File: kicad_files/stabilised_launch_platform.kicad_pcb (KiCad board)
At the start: 2 copper layers, 83.1 x 64.6 mm, 37 parts, among them J1 Conn_01x03_Male, J2 Conn_01x03_Male, J3 Conn_01x06_Male, J4 USB_C_Receptacle_USB2.0, SW1 SW_Push, U1 MAX7375AXR805, U2 AP7370-33Y, U3 STM32L011F3Px, U4 FT201XS, U5 LIS3DH

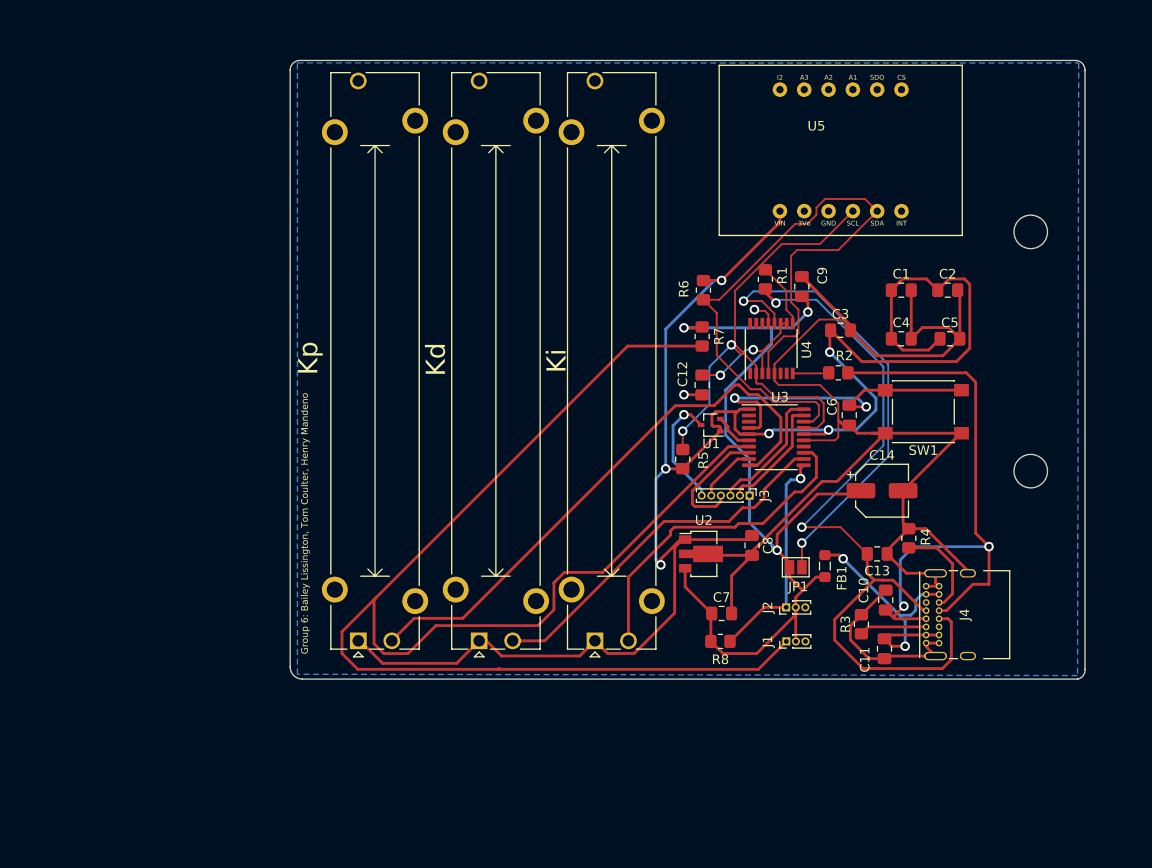
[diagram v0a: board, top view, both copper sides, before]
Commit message: fixed footprints, added mounting holes, fixed traces
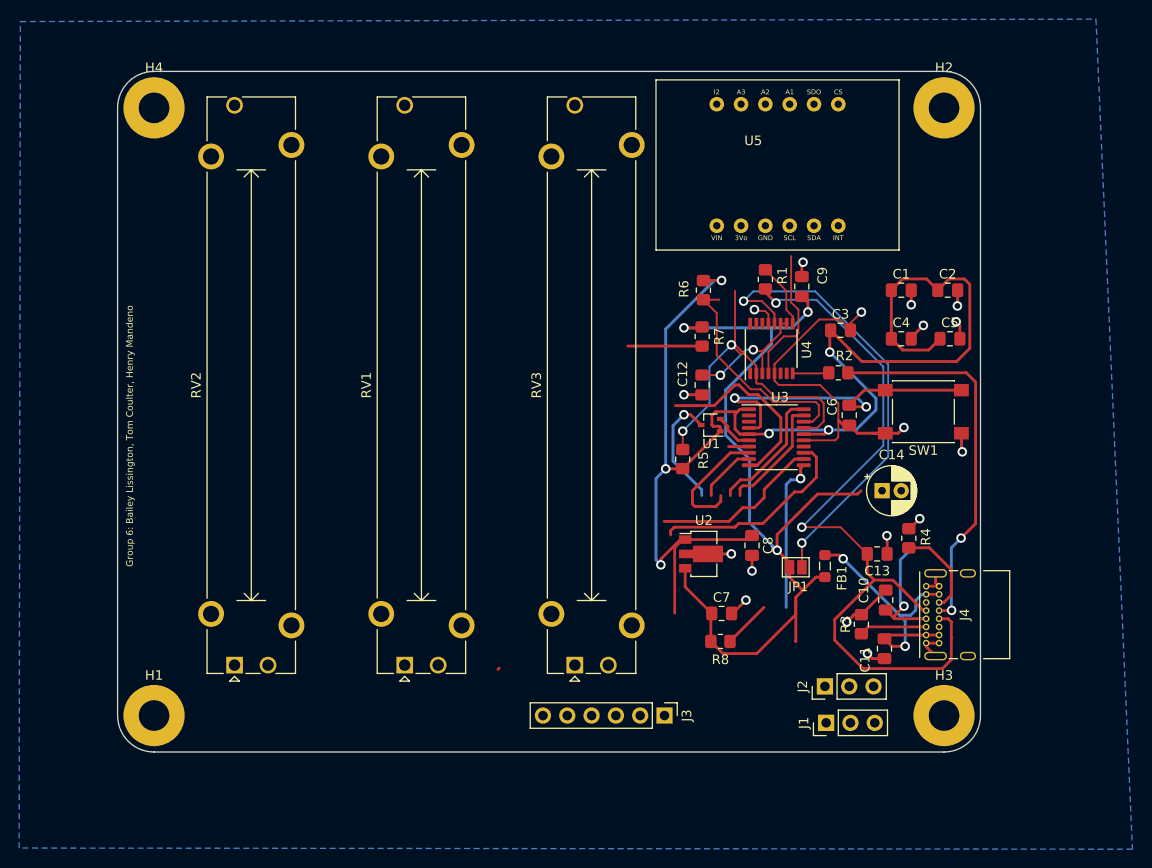
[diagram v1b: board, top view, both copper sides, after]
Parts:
- removed Kd, Ki, Kp: R_Potentiometer, Potentiometer_THT:Potentiometer_Bourns_PTA4543_Single_Slide
- added H1: MountingHole_Pad, MountingHole:MountingHole_3.2mm_M3_Pad, F.Cu at (72.4, 129.5)
- added H2: MountingHole_Pad, MountingHole:MountingHole_3.2mm_M3_Pad, F.Cu at (154.9, 66.0)
- added H3: MountingHole_Pad, MountingHole:MountingHole_3.2mm_M3_Pad, F.Cu at (154.9, 129.5)
- added H4: MountingHole_Pad, MountingHole:MountingHole_3.2mm_M3_Pad, F.Cu at (72.4, 66.0)
- added RV1: R_Potentiometer, Potentiometer_THT:Potentiometer_Bourns_PTA4543_Single_Slide, F.Cu at (98.6, 124.3)
- added RV2: R_Potentiometer, Potentiometer_THT:Potentiometer_Bourns_PTA4543_Single_Slide, F.Cu at (80.8, 124.3)
- added RV3: R_Potentiometer, Potentiometer_THT:Potentiometer_Bourns_PTA4543_Single_Slide, F.Cu at (116.4, 124.3)
- C14: footprint Capacitor_SMD:CP_Elec_5x3 -> Capacitor_THT:CP_Radial_D5.0mm_P2.00mm
- J1, J2: footprint Connector_PinHeader_1.00mm:PinHeader_1x03_P1.00mm_Vertical -> Connector_PinHeader_2.54mm:PinHeader_1x03_P2.54mm_Vertical
- J3: footprint Connector_PinHeader_1.00mm:PinHeader_1x06_P1.00mm_Vertical -> Connector_PinHeader_2.54mm:PinHeader_1x06_P2.54mm_Vertical
- moved J3 24.6 mm to (125.7, 129.5)
- moved J1 9.47 mm to (142.6, 130.3)
- moved J2 9.19 mm to (142.5, 126.5)
- moved U5 6.78 mm to (137.5, 72.0)
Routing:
- net SERVO1_SIG: track 155.8 -> 10.1 mm
- net GND: track 184.9 -> 93.5 mm, vias 3 -> 18
- net +3.3V: track 192.0 -> 143.7 mm
- net POT1: track 60.0 -> 20.2 mm
- net SDA: track 71.2 -> 38.4 mm
- net POT2: track 38.8 -> 17.8 mm
- net SCL: track 53.3 -> 37.5 mm
- net POT3: track 34.5 -> 21.6 mm
- net USBDP: track 63.0 -> 53.3 mm, vias 2 -> 3
- net SERVO2_SIG: track 23.5 -> 21.2 mm
- net Net-(J4-PadB5): track 10.2 -> 9.64 mm
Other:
- board size 83.1 x 64.6 mm -> 90.2 x 71.1 mm

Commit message: PCB routing finished
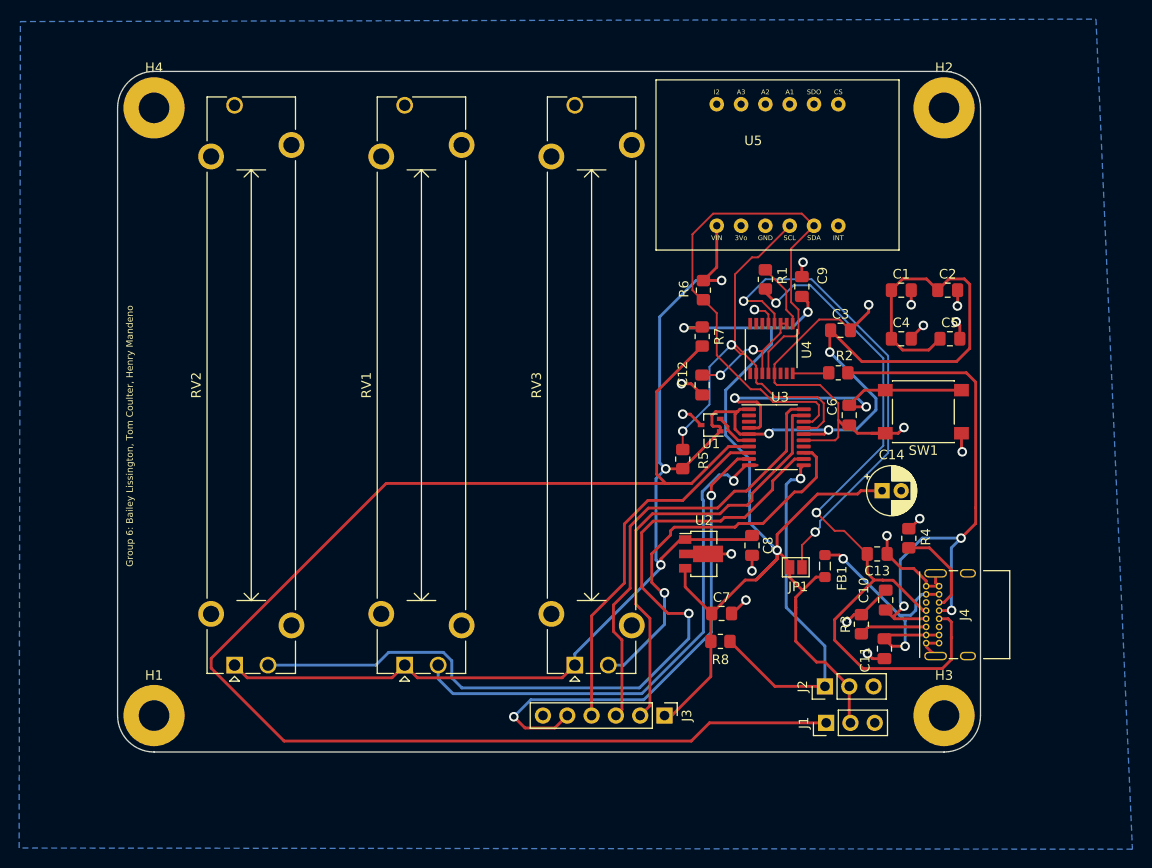
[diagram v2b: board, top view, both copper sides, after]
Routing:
- net SERVO1_SIG: track 10.1 -> 151.6 mm
- net POT2: track 17.8 -> 84.3 mm, vias 0 -> 1
- net +3.3V: track 143.7 -> 195.6 mm
- net MCU_RX: track 6.15 -> 51.3 mm, vias 0 -> 2
- net POT1: track 20.2 -> 54.8 mm, vias 0 -> 1
- net SWDIO: track 12.4 -> 45.6 mm
- net SWCLK: track 13.6 -> 46.6 mm
- net +5V: track 92.5 -> 119.3 mm
- net MCU_TX: track 12.8 -> 37.5 mm
- net SDA: track 38.4 -> 62.4 mm
- net POT3: track 21.6 -> 40.1 mm, vias 0 -> 1
- net SERVO2_SIG: track 21.2 -> 37.9 mm
- net SCL: track 37.5 -> 47.1 mm
- net USBDP: track 53.3 -> 58.6 mm
- net GND: track 93.5 -> 91.2 mm
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
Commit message: added labels, passed drc
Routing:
- net GND: track 91.2 -> 60.6 mm, vias 18 -> 21
- net SCL: track 47.1 -> 45.2 mm
- net +5V: track 119.3 -> 117.8 mm
- net POT1: track 54.8 -> 53.9 mm
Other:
- board text added: "5V"
- board text added: "CLK"
- board text added: "D"
- board text added: "GND"
- board text added: "I"
- board text added: "IO"
- board text added: "P"
- board text added: "RESET"
- board text added: "RX"
- board text added: "SIG"
- board text added: "TX"
- board text added: "X"
- board text added: "Y"
